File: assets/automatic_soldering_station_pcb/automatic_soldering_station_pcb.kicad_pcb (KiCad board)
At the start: 2 copper layers, 25 parts, among them J1 XY_MOS, J2 MAX6675, J3 MAX6675, J4 MAX6675

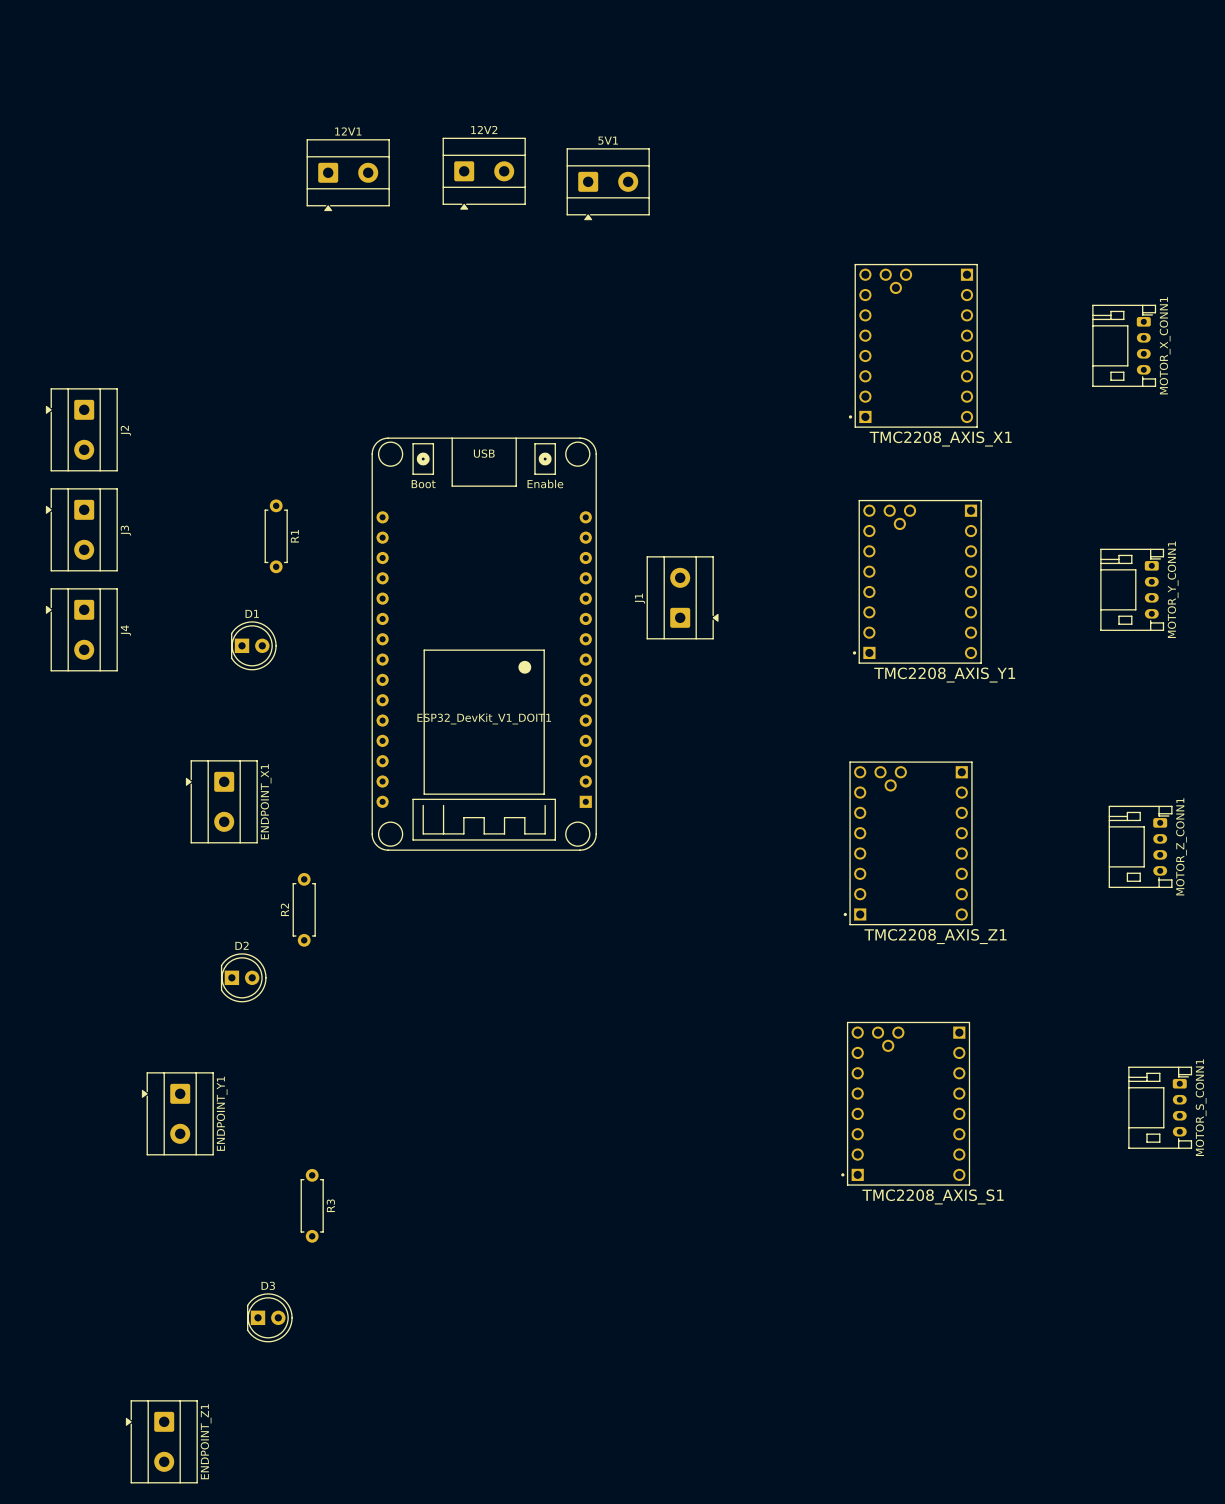
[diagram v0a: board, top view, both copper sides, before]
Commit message: pcb: add autorouted results
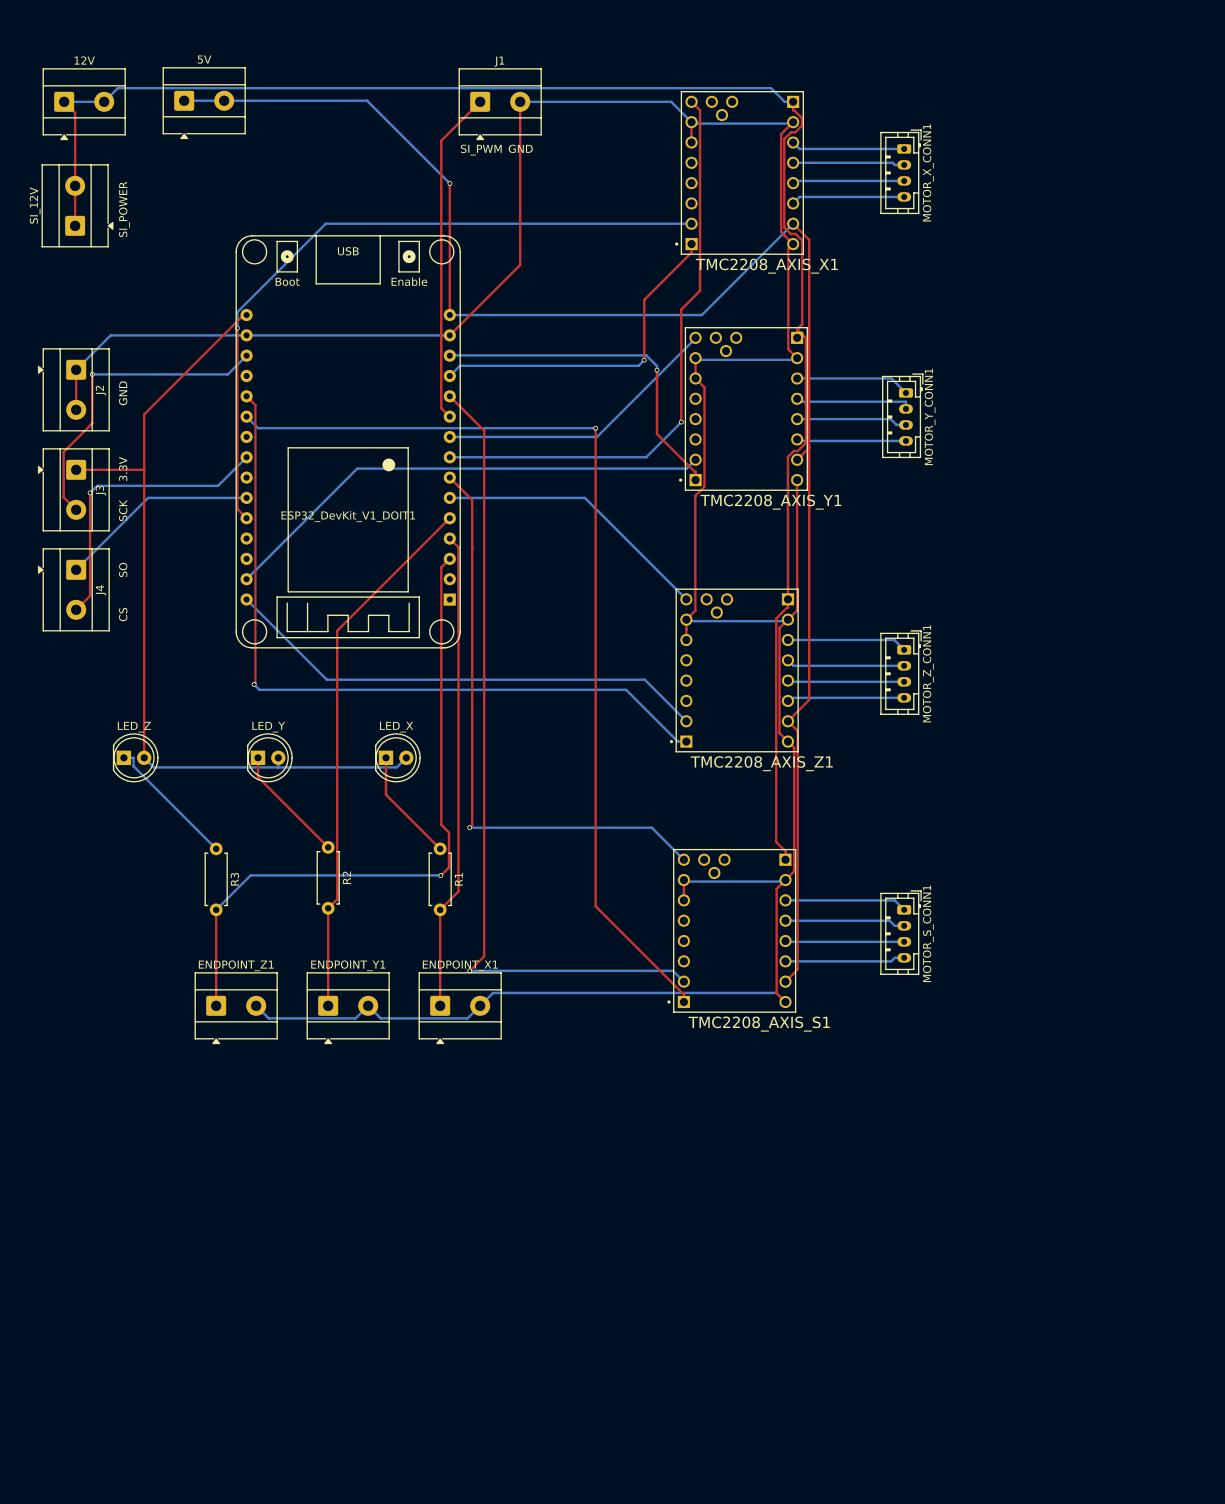
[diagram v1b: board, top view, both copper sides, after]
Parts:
- MOTOR_S_CONN1, MOTOR_X_CONN1, MOTOR_Y_CONN1, MOTOR_Z_CONN1: footprint Connector_JST:JST_PH_S4B-PH-K_1x04_P2.00mm_Horizontal -> Connector_JST:JST_PH_B4B-PH-K_1x04_P2.00mm_Vertical
- R1: value R 10KΩ -> R 1KΩ
- moved LED_Z 72.0 mm to (25.5, 101.0)
- moved J1 69.2 mm to (70.0, 19.0), turned to 0 degrees
- moved ENDPOINT_Z1 52.4 mm to (37.0, 132.0), turned to 0 degrees
- moved 5V 51.5 mm to (33.0, 18.9)
- moved 12V 50.7 mm to (18.0, 19.0)
- moved R1 47.5 mm to (65.0, 112.4)
- moved R3 42.5 mm to (37.0, 112.4)
- moved MOTOR_S_CONN1 40.7 mm to (123.0, 120.0)
- moved ENDPOINT_X1 38.9 mm to (65.0, 132.0), turned to 0 degrees
- moved MOTOR_Z_CONN1 38.6 mm to (123.0, 87.5)
- moved MOTOR_Y_CONN1 37.6 mm to (123.2, 55.4)
- moved MOTOR_X_CONN1 36.9 mm to (123.0, 24.9)
- moved SI_12V 32.3 mm to (19.4, 34.5), turned to 90 degrees
- moved TMC2208_AXIS_S1 30.6 mm to (101.8, 122.6)
- moved TMC2208_AXIS_X1 30.6 mm to (102.8, 27.9)
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- renumbered 12V2 to 12V, 5V1 to 5V, D1 to LED_X, D2 to LED_Y, D3 to LED_Z, 12V1 to SI_12V
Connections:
- LED_X pad 1: GND -> Net-(D1-K)
- LED_X pad 2: /X_ENDPOINT -> +3.3V
- LED_Y pad 1: GND -> Net-(D2-K)
- LED_Y pad 2: /Y_ENDPOINT -> +3.3V
- LED_Z pad 1: GND -> Net-(D3-K)
- LED_Z pad 2: /Z_ENDPOINT -> +3.3V
- R1 pad 1: +3.3V -> Net-(D1-K)
- R2 pad 1: +3.3V -> Net-(D2-K)
- R3 pad 1: +3.3V -> Net-(D3-K)
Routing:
- net GND: track 0.00 -> 371.6 mm
- net +12V: track 0.00 -> 210.6 mm
- net +5V: track 0.00 -> 201.5 mm, vias 0 -> 1
- net /S_DIR: track 0.00 -> 120.6 mm, vias 0 -> 1
- net +3.3V: track 0.00 -> 104.3 mm
- net /S_STEP: track 0.00 -> 101.7 mm, vias 0 -> 1
- net /Z_DIR: track 0.00 -> 93.5 mm, vias 0 -> 1
- net /X_STEP: track 0.00 -> 87.6 mm, vias 0 -> 1
- net /Z_ENDPOINT: track 0.00 -> 83.1 mm, vias 0 -> 1
- net /S_EN: track 0.00 -> 73.8 mm, vias 0 -> 1
- net /X_EN: track 0.00 -> 72.2 mm, vias 0 -> 1
- net /Y_ENDPOINT: track 0.00 -> 67.2 mm
- net /Y_STEP: track 0.00 -> 62.3 mm
- net /Z_STEP: track 0.00 -> 61.3 mm
- net /X_ENDPOINT: track 0.00 -> 59.8 mm
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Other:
- board text added: "3.3V"
- board text added: "CS"
- board text added: "GND"
- board text added: "SCK"
- board text added: "SI_POWER"
- board text added: "SI_PWM"
- board text added: "SO"

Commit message: pcb: add buck converter and reroute pcb manually
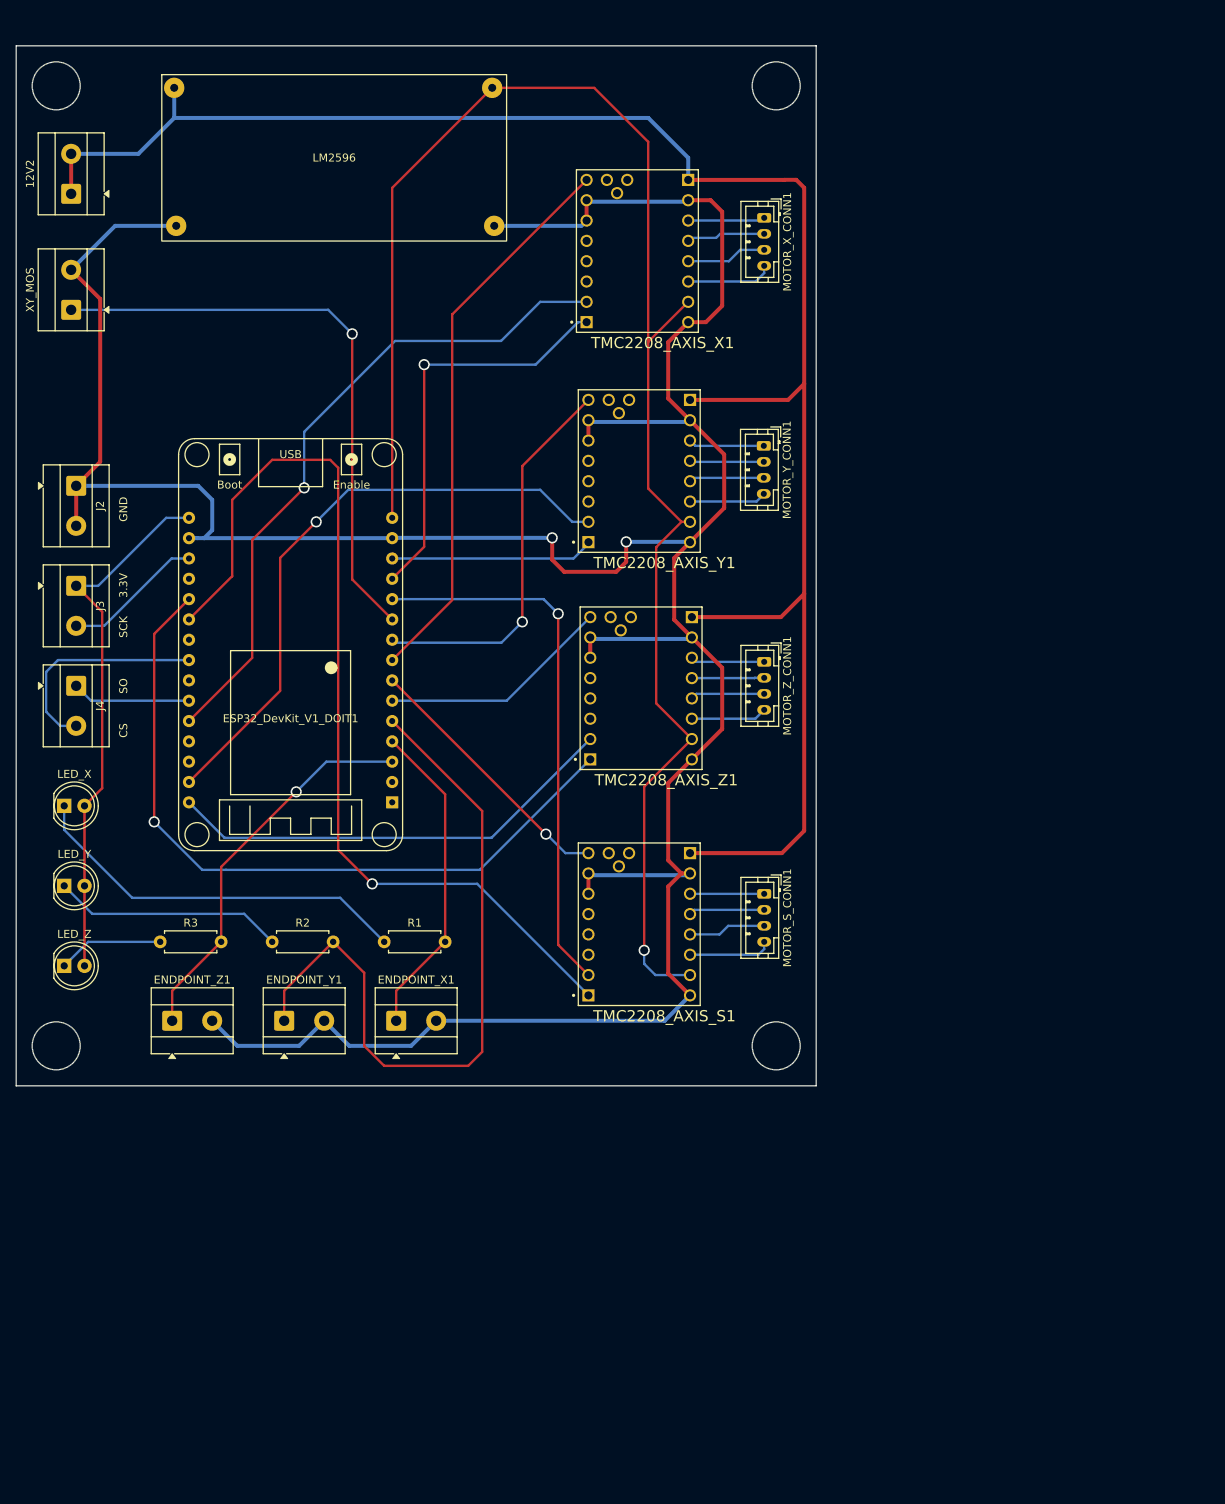
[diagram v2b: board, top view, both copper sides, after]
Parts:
- removed 12V: 12V_INPUT, TerminalBlock_MetzConnect:TerminalBlock_MetzConnect_Type055_RT01502HDWU_1x02_P5.00mm_Horizontal
- removed 5V: 5V_INPUT, TerminalBlock_MetzConnect:TerminalBlock_MetzConnect_Type055_RT01502HDWU_1x02_P5.00mm_Horizontal
- removed J1: XY_MOS, TerminalBlock_MetzConnect:TerminalBlock_MetzConnect_Type055_RT01502HDWU_1x02_P5.00mm_Horizontal
- removed SI_12V: 12V_SOLDERING_POWER, TerminalBlock_MetzConnect:TerminalBlock_MetzConnect_Type055_RT01502HDWU_1x02_P5.00mm_Horizontal
- added 12V2: 12V_Terminal, TerminalBlock_MetzConnect:TerminalBlock_MetzConnect_Type055_RT01502HDWU_1x02_P5.00mm_Horizontal, F.Cu at (18.9, 30.5)
- added LM2596: LM2596, LM2596_Board:LM2596_Board, F.Cu at (51.8, 26.0)
- added XY_MOS: XY_MOS, TerminalBlock_MetzConnect:TerminalBlock_MetzConnect_Type055_RT01502HDWU_1x02_P5.00mm_Horizontal, F.Cu at (18.9, 45.0)
- R1: value R 1KΩ -> R 10KΩ
- moved LED_X 40.7 mm to (18.0, 107.0)
- moved LED_Y 29.0 mm to (18.0, 117.0)
- moved LED_Z 27.0 mm to (18.0, 127.0)
- moved ESP32_DevKit_V1_DOIT1 26.4 mm to (46.3, 106.6)
- moved MOTOR_X_CONN1 19.5 mm to (105.5, 33.5)
- moved MOTOR_Y_CONN1 19.0 mm to (105.5, 62.0)
- moved MOTOR_S_CONN1 17.6 mm to (105.5, 118.0)
- moved MOTOR_Z_CONN1 17.6 mm to (105.5, 89.0)
- moved TMC2208_AXIS_X1 16.4 mm to (89.7, 37.6)
- moved TMC2208_AXIS_Y1 15.5 mm to (89.9, 65.2)
- moved J2 14.5 mm to (19.5, 67.0)
- moved J3 14.5 mm to (19.5, 79.5)
- moved J4 14.5 mm to (19.5, 92.0)
- moved R2 13.7 mm to (44.0, 124.0), turned to 0 degrees
- moved R1 13.6 mm to (58.0, 124.0), turned to 0 degrees
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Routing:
- net /S_EN: track 73.8 -> 33.5 mm
- net +3.3V: track 104.3 -> 67.4 mm
- net Net-(D1-K): track 14.2 -> 48.8 mm
- net /Z_ENDPOINT: track 83.1 -> 48.6 mm
- net /S_STEP: track 101.7 -> 68.2 mm
- net /XY_MOS_PWM: track 41.8 -> 74.1 mm, vias 0 -> 1
- net GND: track 371.6 -> 403.1 mm, vias 0 -> 2
- net +12V: track 210.6 -> 233.6 mm
- net /Y_ENDPOINT: track 67.2 -> 89.5 mm
- net /MAX6675_SCK: track 39.3 -> 17.6 mm, vias 1 -> 0
- net /X_ENDPOINT: track 59.8 -> 40.4 mm
- net /Y_DIR: track 42.8 -> 25.5 mm, vias 1 -> 0
- net /Y_STEP: track 62.3 -> 76.4 mm, vias 0 -> 1
- net Net-(D2-K): track 14.8 -> 28.9 mm
- net /Y_EN: track 35.9 -> 48.7 mm, vias 0 -> 1
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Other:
- board outline added: 100 x 130 mm
- board text removed: "SI_POWER"
- board text removed: "SI_PWM"

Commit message: pcb: polish routing
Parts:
- R1: value R 10KΩ -> R 1KΩ
- renumbered LED_X to D1, LED_Y to D2, LED_Z to D3, XY_MOS to J1
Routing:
- net GND: track 403.1 -> 421.2 mm
- net +12V: track 233.6 -> 244.8 mm
- net +5V: track 205.8 -> 208.9 mm
- net Net-(D2-K): track 28.9 -> 29.9 mm
- net /S_DIR: track 119.5 -> 118.6 mm
- net /Z_DIR: track 92.4 -> 91.6 mm
- net Net-(D3-K): track 13.2 -> 14.0 mm
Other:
- outline, holes or cut-outs redrawn
- board text added: "MAX6675"
